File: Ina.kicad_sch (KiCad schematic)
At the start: 13 parts, among them U601 INA228AQDGSRQ1

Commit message: some
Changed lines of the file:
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@@
       (project "SOC DISPLAY"
         (path "/9f7696f8-e9fa-4362-b2ca-5dde3355ad01/5b884267-8592-446c-85d7-63f10c8d8fbb"
-          (reference "R?") (unit 1)
+          (reference "R608") (unit 1)
         )
       )
@@
       (project "SOC DISPLAY"
         (path "/9f7696f8-e9fa-4362-b2ca-5dde3355ad01/5b884267-8592-446c-85d7-63f10c8d8fbb"
-          (reference "R?") (unit 1)
+          (reference "R601") (unit 1)
         )
       )
@@
       (project "SOC DISPLAY"
         (path "/9f7696f8-e9fa-4362-b2ca-5dde3355ad01/5b884267-8592-446c-85d7-63f10c8d8fbb"
-          (reference "C?") (unit 1)
+          (reference "C603") (unit 1)
         )
       )
@@
   (symbol (lib_id "Device:R") (at 218.44 73.66 0) (unit 1)
     (in_bom yes) (on_board yes) (dnp no)
-    (property "Reference" "R607" (at 217.17 68.58 0)
+    (property "Reference" "R607" (at 215.9 87.63 0)
       (effects (font (size 1.27 1.27)) (justify left))
     )
@@
       (project "SOC DISPLAY"
         (path "/9f7696f8-e9fa-4362-b2ca-5dde3355ad01/5b884267-8592-446c-85d7-63f10c8d8fbb"
-          (reference "R?") (unit 1)
+          (reference "R607") (unit 1)
         )
       )
@@
       (project "SOC DISPLAY"
         (path "/9f7696f8-e9fa-4362-b2ca-5dde3355ad01/5b884267-8592-446c-85d7-63f10c8d8fbb"
-          (reference "C?") (unit 1)
+          (reference "C604") (unit 1)
         )
       )
@@
       (project "SOC DISPLAY"
         (path "/9f7696f8-e9fa-4362-b2ca-5dde3355ad01/5b884267-8592-446c-85d7-63f10c8d8fbb"
-          (reference "C?") (unit 1)
+          (reference "C602") (unit 1)
         )
       )
@@
   (symbol (lib_id "Device:R") (at 214.63 73.66 0) (unit 1)
     (in_bom yes) (on_board yes) (dnp no)
-    (property "Reference" "R606" (at 213.36 68.58 0)
+    (property "Reference" "R606" (at 210.82 68.58 0)
       (effects (font (size 1.27 1.27)) (justify left))
     )
@@
       (project "SOC DISPLAY"
         (path "/9f7696f8-e9fa-4362-b2ca-5dde3355ad01/5b884267-8592-446c-85d7-63f10c8d8fbb"
-          (reference "R?") (unit 1)
+          (reference "R606") (unit 1)
         )
       )
@@
       (project "SOC DISPLAY"
         (path "/9f7696f8-e9fa-4362-b2ca-5dde3355ad01/5b884267-8592-446c-85d7-63f10c8d8fbb"
-          (reference "R?") (unit 1)
+          (reference "R602") (unit 1)
         )
       )
@@
       (project "SOC DISPLAY"
         (path "/9f7696f8-e9fa-4362-b2ca-5dde3355ad01/5b884267-8592-446c-85d7-63f10c8d8fbb"
-          (reference "R?") (unit 1)
+          (reference "R603") (unit 1)
         )
       )
@@
       (project "SOC DISPLAY"
         (path "/9f7696f8-e9fa-4362-b2ca-5dde3355ad01/5b884267-8592-446c-85d7-63f10c8d8fbb"
-          (reference "R?") (unit 1)
+          (reference "R605") (unit 1)
         )
       )
@@
       (project "SOC DISPLAY"
         (path "/9f7696f8-e9fa-4362-b2ca-5dde3355ad01/5b884267-8592-446c-85d7-63f10c8d8fbb"
-          (reference "R?") (unit 1)
+          (reference "R604") (unit 1)
         )
       )
@@
       (project "SOC DISPLAY"
         (path "/9f7696f8-e9fa-4362-b2ca-5dde3355ad01/5b884267-8592-446c-85d7-63f10c8d8fbb"
-          (reference "U?") (unit 1)
+          (reference "U601") (unit 1)
         )
       )
@@
       (project "SOC DISPLAY"
         (path "/9f7696f8-e9fa-4362-b2ca-5dde3355ad01/5b884267-8592-446c-85d7-63f10c8d8fbb"
-          (reference "C?") (unit 1)
-        )
-      )
+          (reference "C601") (unit 1)
+        )
+      )

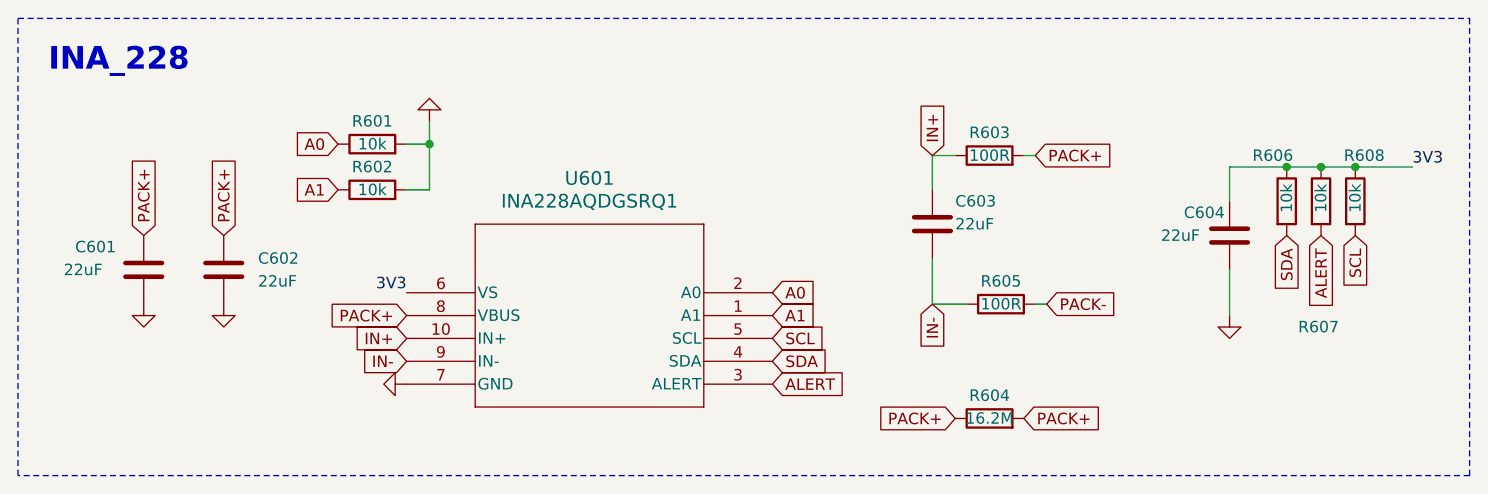
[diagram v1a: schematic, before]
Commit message: make connection between stm and ina and add connectors
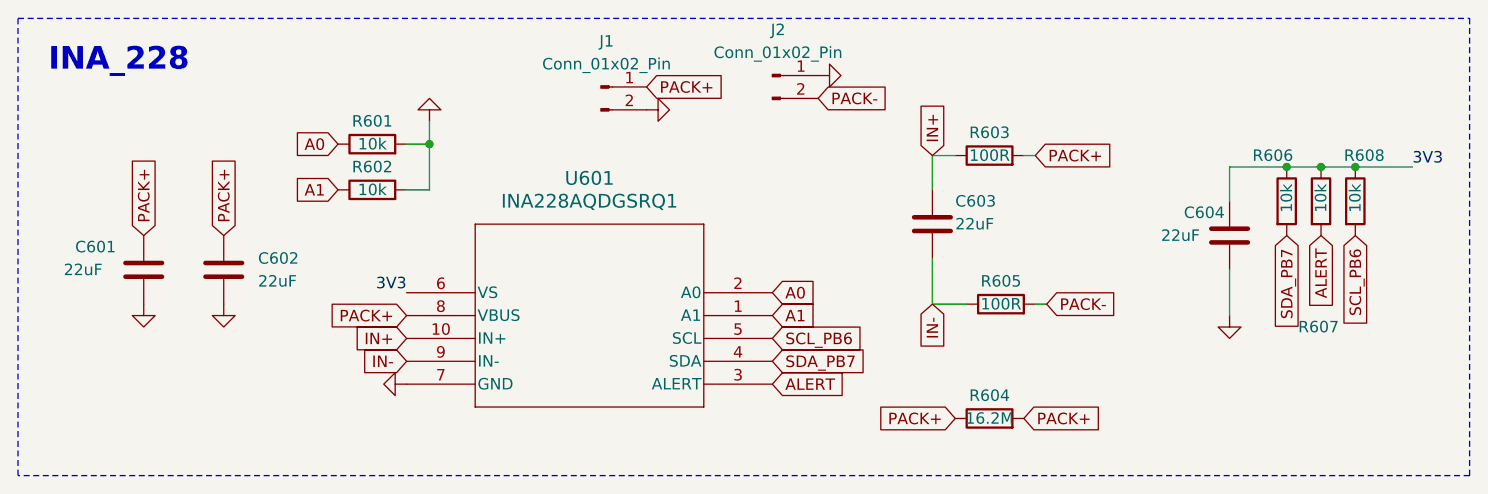
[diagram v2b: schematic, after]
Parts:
- added J1, J2: Conn_01x02_Pin, symbol Connector:Conn_01x02_Pin
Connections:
- net GND: now also J1.2 (Pin_2), J2.1 (Pin_1)
- net PACK+: now also J1.1 (Pin_1)
- net PACK-: now also J2.2 (Pin_2)
- net SCL renamed SCL_PB6
- net SDA renamed SDA_PB7

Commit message: giga
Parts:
- C14: renamed from C601; footprint Capacitor_SMD:C_0201_0603Metric_Pad0.64x0.40mm_HandSolder -> Capacitor_SMD:C_1206_3216Metric_Pad1.33x1.80mm_HandSolder
- C15: renamed from C602; footprint Capacitor_SMD:C_0201_0603Metric_Pad0.64x0.40mm_HandSolder -> Capacitor_SMD:C_1206_3216Metric_Pad1.33x1.80mm_HandSolder
- C16: renamed from C603; footprint Capacitor_SMD:C_0201_0603Metric_Pad0.64x0.40mm_HandSolder -> Capacitor_SMD:C_1206_3216Metric_Pad1.33x1.80mm_HandSolder
- C17: renamed from C604; footprint Capacitor_SMD:C_0201_0603Metric_Pad0.64x0.40mm_HandSolder -> Capacitor_SMD:C_1206_3216Metric_Pad1.33x1.80mm_HandSolder
- J6: renamed from J1; footprint (none) -> TerminalBlock:TerminalBlock_bornier-2_P5.08mm
- J7: renamed from J2; footprint (none) -> TerminalBlock:TerminalBlock_bornier-2_P5.08mm
- R35: renamed from R601; footprint Capacitor_SMD:C_0201_0603Metric_Pad0.64x0.40mm_HandSolder -> Resistor_SMD:R_0603_1608Metric_Pad0.98x0.95mm_HandSolder
- R36: renamed from R602; footprint Capacitor_SMD:C_0201_0603Metric_Pad0.64x0.40mm_HandSolder -> Resistor_SMD:R_0603_1608Metric_Pad0.98x0.95mm_HandSolder
- R37: renamed from R603; footprint Capacitor_SMD:C_0201_0603Metric_Pad0.64x0.40mm_HandSolder -> Resistor_SMD:R_0603_1608Metric_Pad0.98x0.95mm_HandSolder
- R38: renamed from R604; footprint Capacitor_SMD:C_0201_0603Metric_Pad0.64x0.40mm_HandSolder -> Resistor_SMD:R_0603_1608Metric_Pad0.98x0.95mm_HandSolder
- R39: renamed from R605; footprint Capacitor_SMD:C_0201_0603Metric_Pad0.64x0.40mm_HandSolder -> Resistor_SMD:R_0603_1608Metric_Pad0.98x0.95mm_HandSolder
- R40: renamed from R606; footprint Capacitor_SMD:C_0201_0603Metric_Pad0.64x0.40mm_HandSolder -> Resistor_SMD:R_0603_1608Metric_Pad0.98x0.95mm_HandSolder
- R41: renamed from R607; footprint Capacitor_SMD:C_0201_0603Metric_Pad0.64x0.40mm_HandSolder -> Resistor_SMD:R_0603_1608Metric_Pad0.98x0.95mm_HandSolder
- R42: renamed from R608; footprint Capacitor_SMD:C_0201_0603Metric_Pad0.64x0.40mm_HandSolder -> Resistor_SMD:R_0603_1608Metric_Pad0.98x0.95mm_HandSolder
- renumbered U601 to U6
